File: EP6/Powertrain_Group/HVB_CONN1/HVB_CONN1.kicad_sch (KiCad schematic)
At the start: 18 parts, among them J1 HVBLV1, J10 IMD_RESET, J11 BSPD_RESET, J12 BSPDTinbox, J13 Oil Pressure, J14 SCout, J15 DASH_IND, J16 BSPDT, J17 TSSI_RTML, J18 toACC, J19 BL_BAK, J2 PWRfromLVBAT, J3 PWRout, J4 PWRout, J6 SCinterlock1, J7 SCinterlock2, J8 SCinterlock3, J9 BMS_RESET

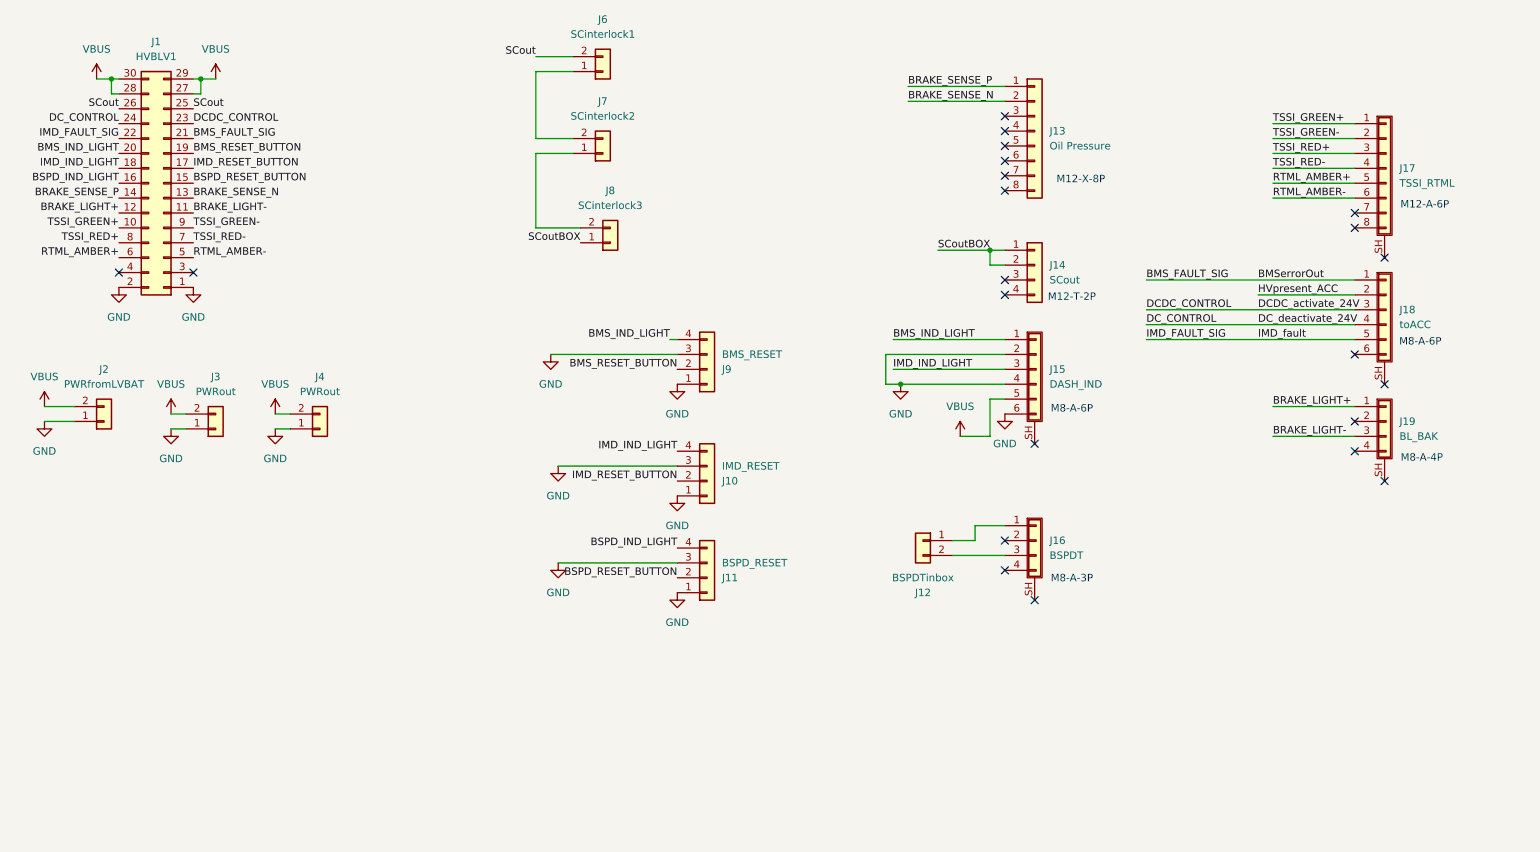
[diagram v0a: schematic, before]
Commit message: update HVB_CONN1 to V1.1
V1.1 change TSSI_RTML connector pinout to match 6p connector (5->6, 6->7)
     change dash SB light power source
     change reset button connector to JST 2.0
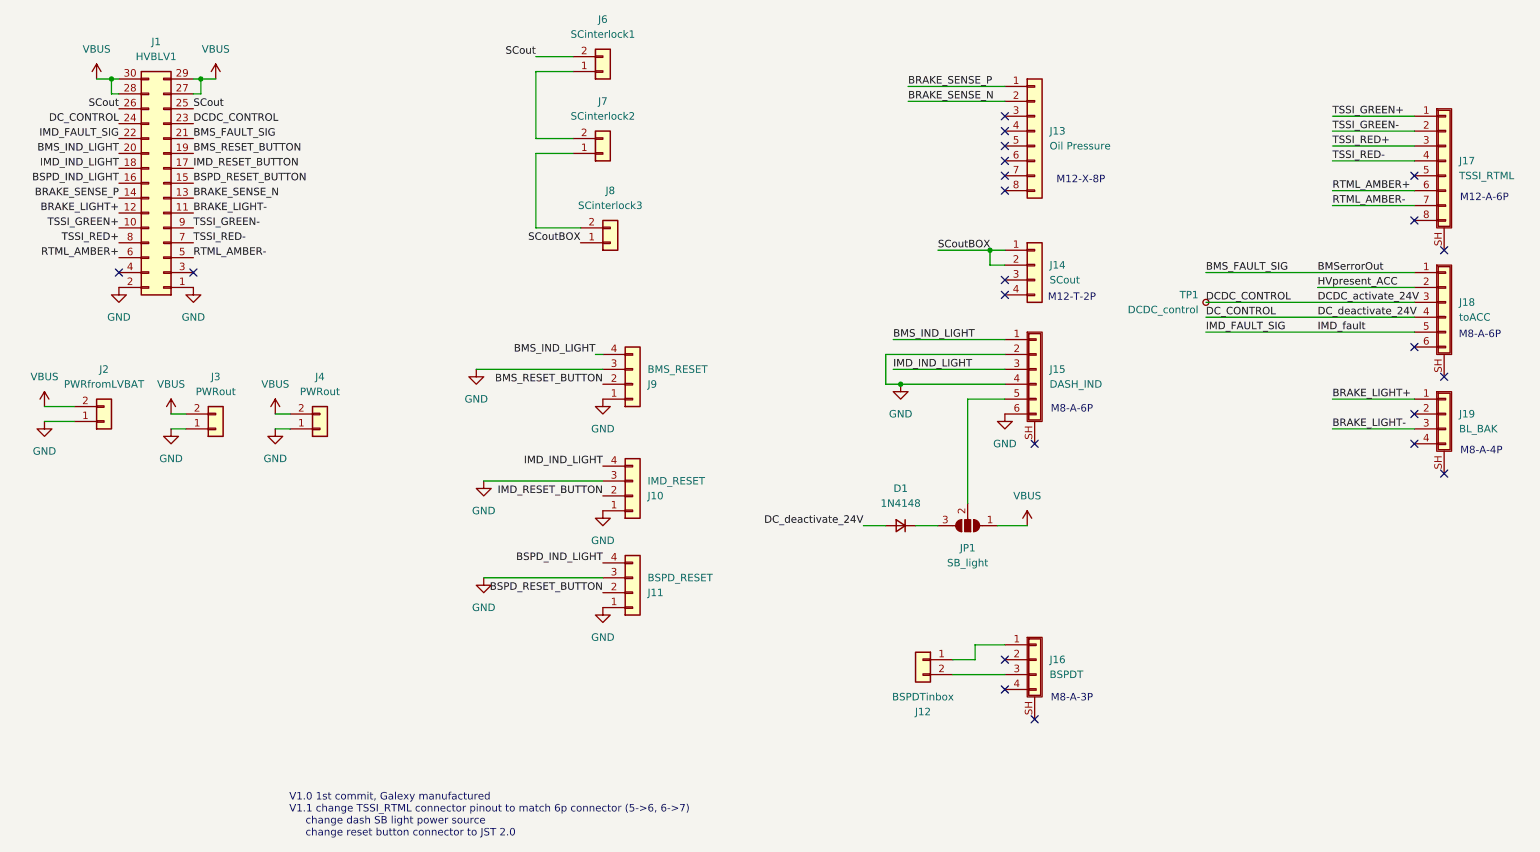
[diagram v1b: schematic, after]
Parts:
- added D1: 1N4148, Diode_SMD:D_SOD-323_HandSoldering, symbol Device:D_Small
- added JP1: SB_light, Jumper:SolderJumper-3_P1.3mm_Open_RoundedPad1.0x1.5mm, symbol Jumper:SolderJumper_3_Open
- added TP1: DCDC_control, TestPoint:TestPoint_Pad_D1.0mm, symbol Connector:TestPoint_Small
- J10, J11, J9: footprint Connector_JST:JST_XH_B4B-XH-A_1x04_P2.50mm_Vertical -> Connector_JST:JST_PH_B4B-PH-K_1x04_P2.00mm_Vertical
- J12: footprint Connector_JST:JST_XH_B2B-XH-A_1x02_P2.50mm_Vertical -> Connector_JST:JST_PH_B2B-PH-K_1x02_P2.00mm_Vertical
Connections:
- net DCDC_CONTROL: now also TP1.1
- net DC_CONTROL: now also D1.2 (A)
- net RTML_AMBER+: now also J17.6 (Pin_6); no longer J17.5 (Pin_5)
- net RTML_AMBER-: now also J17.7 (Pin_7); no longer J17.6 (Pin_6)
- net VBUS: now also JP1.1 (A); no longer J15.5 (Pin_5)
- new net: D1.1 (K), JP1.3 (B)
- new net: J15.5 (Pin_5), JP1.2 (C)
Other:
- note added: "V1.0 1st commit, Galexy manufactured V1.1 change TSSI_RTML connector pinout to match 6p connector (5->6, 6->7) change dash SB light power source change reset button connector to JST 2.0"
- moved on the sheet: J10, J11, J12, J16, J17, J18, J19, J9
